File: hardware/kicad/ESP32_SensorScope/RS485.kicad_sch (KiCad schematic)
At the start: 27 parts, among them J1 RS485_A, J2 RS485_B, J3 RS485_A, J4 RS485_B, Q1 PMOS, Q2 NMOS, U3 SN74LV1T125DBV, U4 SP3481CN OR SN65HVD485E, U5 ASSR-1218

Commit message: Various changes
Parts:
- removed D1, D2: D_Schottky, symbol Device:D_Schottky
- removed J3: RS485_A, symbol Connector:Conn_01x01_Socket
- removed J4: RS485_B, symbol Connector:Conn_01x01_Socket
- removed Q1: PMOS, symbol Simulation_SPICE:PMOS
- removed Q2: NMOS, symbol Simulation_SPICE:NMOS
- removed R10, R11: 60, symbol Device:R
- removed R12, R13: 10, symbol Device:R
- removed R7, R9: 750, symbol Device:R
- removed R8: 10K, symbol Device:R
- added D13, D14: D_Schottky, symbol Device:D_Schottky
- added F2: Polyfuse, symbol Device:Polyfuse
- added Q4: PMOS, symbol Simulation_SPICE:PMOS
- added Q5, Q6: NMOS, symbol Simulation_SPICE:NMOS
- added R46: 10K, symbol Device:R
- added R47, R48: 60, symbol Device:R
- added R49: 470, symbol Device:R
- R5, R6: value 10 -> 750
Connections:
- net +5V: now also Q4.3 (S), R46.1
- net GND: now also U5.2, Q5.3 (S), Q6.3 (S)
- net at R4.1, R6.1, U4.7 (B): now also U5.3, F2.1
- net at J2.1 (Pin_1): now also F2.2; no longer R6.2
- net at J1.1 (Pin_1): now also F1.2; no longer R5.2
- net at R4.2, U4.6 (A): now also F1.1, R5.2, R47.1; no longer R5.1
- net at U5.4: now also R48.2; no longer F1.1
- net at U5.1: now also R49.1
- new net: Q4.2 (G), Q6.1 (D), R46.2
- new net: R47.2, R48.1
- new net: D14.2 (A), R6.2
- new net: D13.2 (A), Q4.1 (D)
- new net: D14.1 (K), Q5.1 (D)
- new net: D13.1 (K), R5.1
- new net RS485_Bias_EN: Q5.2 (G), Q6.2 (G)
- new net RS485_TerminationR: R49.2
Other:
- moved on the sheet: C2, F1, J1, J2, U5

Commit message: something probobly
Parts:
- removed R3: 10K, symbol Device:R
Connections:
- net RS485_TX_nEN is gone; now on net RS485_EN: U4.3 (DE)
- net RS485_EN: now reaches U4.2 (~{RE})
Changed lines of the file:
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@@
 	(paper "A4")
+	(junction
+		(at 114.3 92.71)
+		(diameter 0)
+		(color 0 0 0 0)
+	)
 	(junction
 		(at 142.24 92.71)
@@
 	(wire
 		(pts
-			(xy 105.41 90.17) (xy 106.68 90.17)
-		)
-		(stroke
-			(width 0)
-			(type default)
-		)
-	)
-	(wire
-		(pts
 			(xy 137.16 85.09) (xy 137.16 82.55)
 		)
@@
 	(wire
 		(pts
-			(xy 96.52 92.71) (xy 116.84 92.71)
+			(xy 96.52 92.71) (xy 114.3 92.71)
 		)
 		(stroke
@@
 	(wire
 		(pts
+			(xy 114.3 90.17) (xy 114.3 92.71)
+		)
+		(stroke
+			(width 0)
+			(type default)
+		)
+	)
+	(wire
+		(pts
 			(xy 137.16 82.55) (xy 142.24 82.55)
 		)
@@
 		(pts
 			(xy 115.57 81.28) (xy 115.57 87.63)
+		)
+		(stroke
+			(width 0)
+			(type default)
+		)
+	)
+	(wire
+		(pts
+			(xy 114.3 92.71) (xy 116.84 92.71)
 		)
 		(stroke
@@
 		)
 	)
-	(global_label "RS485_TX_nEN"
+	(global_label "RS485_EN"
 		(shape input)
 		(at 96.52 92.71 180)
@@
 		)
 		(property "Intersheetrefs" "${INTERSHEET_REFS}"
-			(at 79.686 92.71 0)
+			(at 83.9797 92.71 0)
 			(effects
 				(font
@@
 				(justify right)
 				(hide yes)
-			)
-		)
-	)
-	(symbol
-		(lib_id "Device:R")
-		(at 110.49 90.17 90)
-		(unit 1)
-		(exclude_from_sim no)
-		(in_bom yes)
-		(on_board yes)
-		(dnp no)
-		(property "Reference" "R3"
-			(at 110.49 90.17 90)
-			(effects
-				(font
-					(size 1.27 1.27)
-				)
-			)
-		)
-		(property "Value" "10K"
-			(at 110.49 88.138 90)
-			(effects
-				(font
-					(size 1.27 1.27)
-				)
-			)
-		)
-		(property "Footprint" ""
-			(at 110.49 91.948 90)
-			(effects
-				(font
-					(size 1.27 1.27)
-				)
-				(hide yes)
-			)
-		)
-		(property "Datasheet" "~"
-			(at 110.49 90.17 0)
-			(effects
-				(font
-					(size 1.27 1.27)
-				)
-				(hide yes)
-			)
-		)
-		(property "Description" "Resistor"
-			(at 110.49 90.17 0)
-			(effects
-				(font
-					(size 1.27 1.27)
-				)
-				(hide yes)
-			)
-		)
-		(pin "1"
-		)
-		(pin "2"
-		)
-		(instances
-			(project "ESP32_SensorScope"
-				(path "/53b18f60-802b-4114-ad1b-2672cfed64a1/023aa14c-98ee-4b74-98c6-de8e26121a9a"
-					(reference "R3")
-					(unit 1)
-				)
 			)
 		)
@@
 					(unit 1)
 				)
-			)
-		)
-	)
-	(symbol
-		(lib_id "power:GND")
-		(at 105.41 90.17 270)
-		(unit 1)
-		(exclude_from_sim no)
-		(in_bom yes)
-		(on_board yes)
-		(dnp no)
-		(fields_autoplaced yes)
-		(property "Reference" "#PWR05"
-			(at 99.06 90.17 0)
-			(effects
-				(font
-					(size 1.27 1.27)
-				)
-				(hide yes)
-			)
-		)
-		(property "Value" "GND"
-			(at 101.6 90.1699 90)
-			(effects
-				(font
-					(size 1.27 1.27)
-				)
-				(justify right)
-			)
-		)
-		(property "Footprint" ""
-			(at 105.41 90.17 0)
-			(effects
-				(font
-					(size 1.27 1.27)
-				)
-				(hide yes)
-			)
-		)
-		(property "Datasheet" ""
-			(at 105.41 90.17 0)
-			(effects
-				(font
-					(size 1.27 1.27)
-				)
-				(hide yes)
-			)
-		)
-		(property "Description" "Power symbol creates a global label with name \"GND\" , ground"
-			(at 105.41 90.17 0)
-			(effects
-				(font
-					(size 1.27 1.27)
-				)
-				(hide yes)
-			)
-		)
-		(pin "1"
-		)
-		(instances
-			(project "ESP32_SensorScope"
-				(path "/53b18f60-802b-4114-ad1b-2672cfed64a1/023aa14c-98ee-4b74-98c6-de8e26121a9a"
-					(reference "#PWR05")
-					(unit 1)
-				)

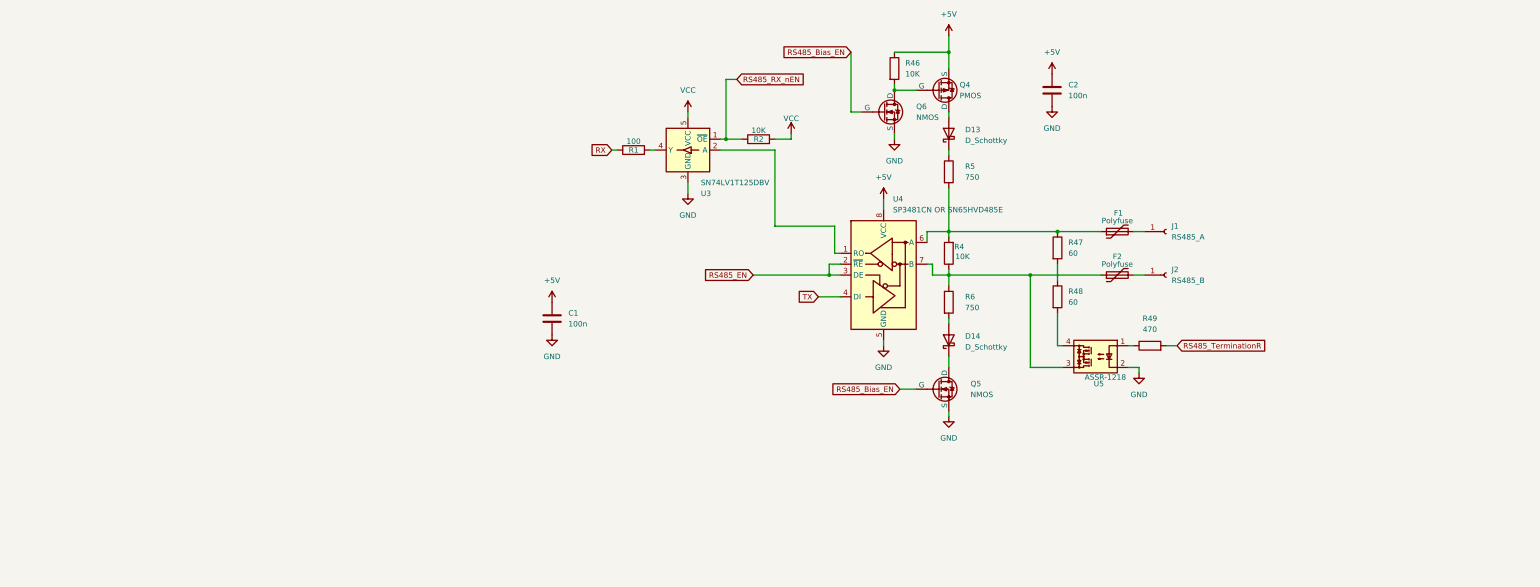
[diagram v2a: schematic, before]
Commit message: som updates on the schematics
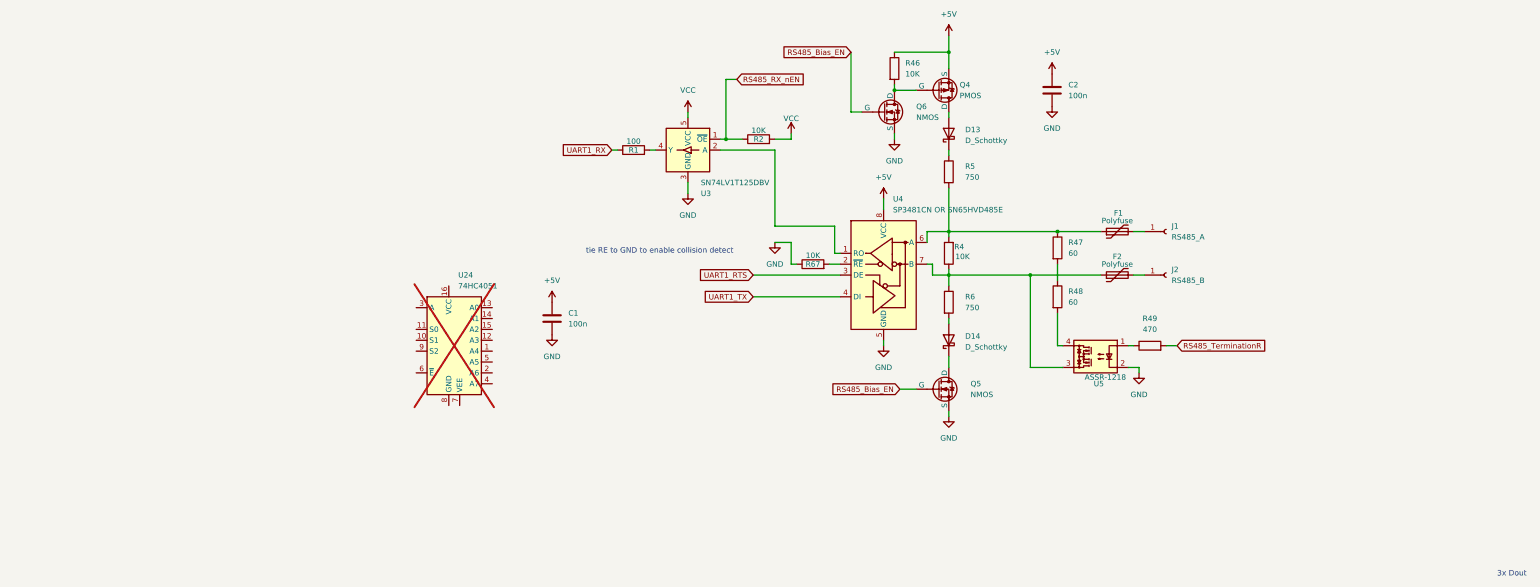
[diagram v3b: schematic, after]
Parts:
- added R67: 10K, symbol Device:R
- added U24: 74HC4051, symbol 74xx:74HC4051
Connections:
- net GND: now also R67.1
- net RS485_EN: no longer names the net of U4.2 (~{RE})
- net RS485_EN: now also R67.2; no longer U4.3 (DE)
- net RX renamed UART1_RX
- net TX renamed UART1_TX
- new net UART1_RTS: U4.3 (DE)
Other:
- note added: "3x Dout"
- note added: "tie RE to GND to enable collision detect"

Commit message: updatet schematic
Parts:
- removed J1: RS485_A, symbol Connector:Conn_01x01_Socket
- removed J2: RS485_B, symbol Connector:Conn_01x01_Socket
- removed U24: 74HC4051, symbol 74xx:74HC4051
- added D33, D34: 28VDC, symbol Device:D_TVS
- added R26, R27: 30, symbol Device:R
- R47, R48: value 60 -> 30
- U4: value SP3481CN OR SN65HVD485E -> SP3481CN OR SN65HVD485E OR THVD24x0(±70V)
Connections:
- net GND: now also D33.1 (A1), D34.1 (A1)
- net RS485_D+: now reaches F1.2
- net at F1.1, R4.2, R47.1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: now also D33.2 (A2)
- net at R47.2: now also R27.1; no longer R48.1
- net at F2.1, R4.1, R6.1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: now also R48.1, D34.2 (A2); no longer U5.3
- net RS485_D-: now reaches F2.2
- net at R48.2: now also R26.1; no longer U5.4
- new net: R26.2, U5.3
- new net: R27.2, U5.4
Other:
- moved on the sheet: C1, C2, F1, F2, R47, R48, R49, U5

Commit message: addet some footprints"
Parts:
- C1, C2: footprint (none) -> Capacitor_SMD:C_0805_2012Metric
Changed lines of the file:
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@@
 			)
 		)
-		(property "Footprint" ""
+		(property "Footprint" "Capacitor_SMD:C_0805_2012Metric"
 			(at 54.3052 45.72 0)
 			(effects
@@
 			)
 		)
-		(property "Footprint" ""
+		(property "Footprint" "Capacitor_SMD:C_0805_2012Metric"
 			(at 96.2152 120.65 0)
 			(effects
